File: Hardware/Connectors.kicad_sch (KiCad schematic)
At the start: 22 parts, among them J1 Conn_01x07, J2 Conn_01x03, SW6 SW_Push, SW7 SW_Push

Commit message: Replaced the ISOW1044 CAN Transceiver with the ISO1042 + isolated DC-DC and LDO
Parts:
- renumbered C28 to C22, C29 to C23, FILTER2 to FILTER1, J2 to J1, J1 to J2, R16 to R14, R17 to R15, R13 to R16, R15 to R17, R14 to R18, R18 to R19, TVS5 to TVS3, TVS3 to TVS4, TVS4 to TVS5
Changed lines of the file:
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@@
 		(dnp no)
 		(fields_autoplaced yes)
-		(property "Reference" "#PWR022"
+		(property "Reference" "#PWR024"
 			(at 73.66 198.12 0)
 			(effects
@@
 			(project "CANIO-Board"
 				(path "/a11f98b2-3b09-4cf9-8535-19e509fe91b9/e5b74127-3612-4017-b1e2-26fb10a2adfa"
-					(reference "#PWR022")
+					(reference "#PWR024")
 					(unit 1)
 				)
@@
 		(on_board yes)
 		(dnp no)
-		(property "Reference" "R13"
+		(property "Reference" "R16"
 			(at 40.64 181.61 90)
 			(effects
@@
 			(project "CANIO-Board"
 				(path "/a11f98b2-3b09-4cf9-8535-19e509fe91b9/e5b74127-3612-4017-b1e2-26fb10a2adfa"
-					(reference "R13")
+					(reference "R16")
 					(unit 1)
 				)
@@
 		(dnp no)
 		(fields_autoplaced yes)
-		(property "Reference" "#PWR023"
+		(property "Reference" "#PWR019"
 			(at 118.11 105.41 0)
 			(effects
@@
 			(project "CANIO-Board"
 				(path "/a11f98b2-3b09-4cf9-8535-19e509fe91b9/e5b74127-3612-4017-b1e2-26fb10a2adfa"
-					(reference "#PWR023")
+					(reference "#PWR019")
 					(unit 1)
 				)
@@
 		(dnp no)
 		(fields_autoplaced yes)
-		(property "Reference" "#PWR021"
+		(property "Reference" "#PWR022"
 			(at 59.69 148.59 0)
 			(effects
@@
 			(project "CANIO-Board"
 				(path "/a11f98b2-3b09-4cf9-8535-19e509fe91b9/e5b74127-3612-4017-b1e2-26fb10a2adfa"
-					(reference "#PWR021")
+					(reference "#PWR022")
 					(unit 1)
 				)
@@
 		(on_board yes)
 		(dnp no)
-		(property "Reference" "R16"
+		(property "Reference" "R14"
 			(at 219.456 66.294 90)
 			(effects
@@
 			(project ""
 				(path "/a11f98b2-3b09-4cf9-8535-19e509fe91b9/e5b74127-3612-4017-b1e2-26fb10a2adfa"
-					(reference "R16")
+					(reference "R14")
 					(unit 1)
 				)
@@
 		(dnp no)
 		(fields_autoplaced yes)
-		(property "Reference" "#PWR024"
+		(property "Reference" "#PWR023"
 			(at 132.08 165.1 0)
 			(effects
@@
 			(project "CANIO-Board"
 				(path "/a11f98b2-3b09-4cf9-8535-19e509fe91b9/e5b74127-3612-4017-b1e2-26fb10a2adfa"
-					(reference "#PWR024")
+					(reference "#PWR023")
 					(unit 1)
 				)
@@
 		(on_board yes)
 		(dnp no)
-		(property "Reference" "#PWR025"
+		(property "Reference" "#PWR021"
 			(at 232.41 111.76 0)
 			(effects
@@
 			(project "CANIO-Board"
 				(path "/a11f98b2-3b09-4cf9-8535-19e509fe91b9/e5b74127-3612-4017-b1e2-26fb10a2adfa"
-					(reference "#PWR025")
+					(reference "#PWR021")
 					(unit 1)
 				)
@@
 		(dnp no)
 		(fields_autoplaced yes)
-		(property "Reference" "C28"
+		(property "Reference" "C22"
 			(at 50.8 172.8469 0)
 			(effects
@@
 			(project "CANIO-Board"
 				(path "/a11f98b2-3b09-4cf9-8535-19e509fe91b9/e5b74127-3612-4017-b1e2-26fb10a2adfa"
-					(reference "C28")
+					(reference "C22")
 					(unit 1)
 				)
@@
 		(dnp no)
 		(fields_autoplaced yes)
-		(property "Reference" "J1"
+		(property "Reference" "J2"
 			(at 74.93 71.1199 0)
 			(effects
@@
 			(project ""
 				(path "/a11f98b2-3b09-4cf9-8535-19e509fe91b9/e5b74127-3612-4017-b1e2-26fb10a2adfa"
-					(reference "J1")
+					(reference "J2")
 					(unit 1)
 				)
@@
 		(on_board yes)
 		(dnp no)
-		(property "Reference" "J2"
+		(property "Reference" "J1"
 			(at 129.794 60.452 0)
 			(effects
@@
 			(project ""
 				(path "/a11f98b2-3b09-4cf9-8535-19e509fe91b9/e5b74127-3612-4017-b1e2-26fb10a2adfa"
-					(reference "J2")
+					(reference "J1")
 					(unit 1)
 				)
@@
 		(on_board yes)
 		(dnp no)
-		(property "Reference" "R14"
+		(property "Reference" "R18"
 			(at 52.07 181.61 0)
 			(effects
@@
 			(project "CANIO-Board"
 				(path "/a11f98b2-3b09-4cf9-8535-19e509fe91b9/e5b74127-3612-4017-b1e2-26fb10a2adfa"
-					(reference "R14")
+					(reference "R18")
 					(unit 1)
 				)
@@
 		(on_board yes)
 		(dnp no)
-		(property "Reference" "TVS4"
+		(property "Reference" "TVS5"
 			(at 68.326 91.44 0)
 			(effects
@@
 			(project ""
 				(path "/a11f98b2-3b09-4cf9-8535-19e509fe91b9/e5b74127-3612-4017-b1e2-26fb10a2adfa"
-					(reference "TVS4")
+					(reference "TVS5")
 					(unit 1)
 				)
@@
 		(on_board yes)
 		(dnp no)
-		(property "Reference" "TVS3"
+		(property "Reference" "TVS4"
 			(at 39.878 91.186 0)
 			(effects
@@
 			(project "CANIO-Board"
 				(path "/a11f98b2-3b09-4cf9-8535-19e509fe91b9/e5b74127-3612-4017-b1e2-26fb10a2adfa"
-					(reference "TVS3")
+					(reference "TVS4")
 					(unit 1)
 				)
@@
 		(on_board yes)
 		(dnp no)
-		(property "Reference" "R18"
+		(property "Reference" "R19"
 			(at 52.07 186.69 0)
 			(effects
@@
 			(project "CANIO-Board"
 				(path "/a11f98b2-3b09-4cf9-8535-19e509fe91b9/e5b74127-3612-4017-b1e2-26fb10a2adfa"
-					(reference "R18")
+					(reference "R19")
 					(unit 1)
 				)
@@
 		(on_board yes)
 		(dnp no)
-		(property "Reference" "TVS5"
+		(property "Reference" "TVS3"
 			(at 134.366 90.17 0)
 			(effects
@@
 			(project "CANIO-Board"
 				(path "/a11f98b2-3b09-4cf9-8535-19e509fe91b9/e5b74127-3612-4017-b1e2-26fb10a2adfa"
-					(reference "TVS5")
+					(reference "TVS3")
 					(unit 1)
 				)
@@
 		(on_board yes)
 		(dnp no)
-		(property "Reference" "R15"
+		(property "Reference" "R17"
 			(at 73.66 176.53 90)
 			(effects
@@
 			(project "CANIO-Board"
 				(path "/a11f98b2-3b09-4cf9-8535-19e509fe91b9/e5b74127-3612-4017-b1e2-26fb10a2adfa"
-					(reference "R15")
+					(reference "R17")
 					(unit 1)
 				)
@@
 		(dnp no)
 		(fields_autoplaced yes)
-		(property "Reference" "C29"
+		(property "Reference" "C23"
 			(at 82.55 184.2769 0)
 			(effects
@@
 			(project "CANIO-Board"
 				(path "/a11f98b2-3b09-4cf9-8535-19e509fe91b9/e5b74127-3612-4017-b1e2-26fb10a2adfa"
-					(reference "C29")
+					(reference "C23")
 					(unit 1)
 				)
@@
 		(dnp no)
 		(fields_autoplaced yes)
-		(property "Reference" "FILTER2"
+		(property "Reference" "FILTER1"
 			(at 196.85 74.93 0)
 			(effects
@@
 			(project ""
 				(path "/a11f98b2-3b09-4cf9-8535-19e509fe91b9/e5b74127-3612-4017-b1e2-26fb10a2adfa"
-					(reference "FILTER2")
+					(reference "FILTER1")
 					(unit 1)
 				)
@@
 		(on_board yes)
 		(dnp no)
-		(property "Reference" "R17"
+		(property "Reference" "R15"
 			(at 219.456 68.834 90)
 			(effects
@@
 			(project "CANIO-Board"
 				(path "/a11f98b2-3b09-4cf9-8535-19e509fe91b9/e5b74127-3612-4017-b1e2-26fb10a2adfa"
-					(reference "R17")
-					(unit 1)
-				)
+					(reference "R15")
+					(unit 1)
+				)

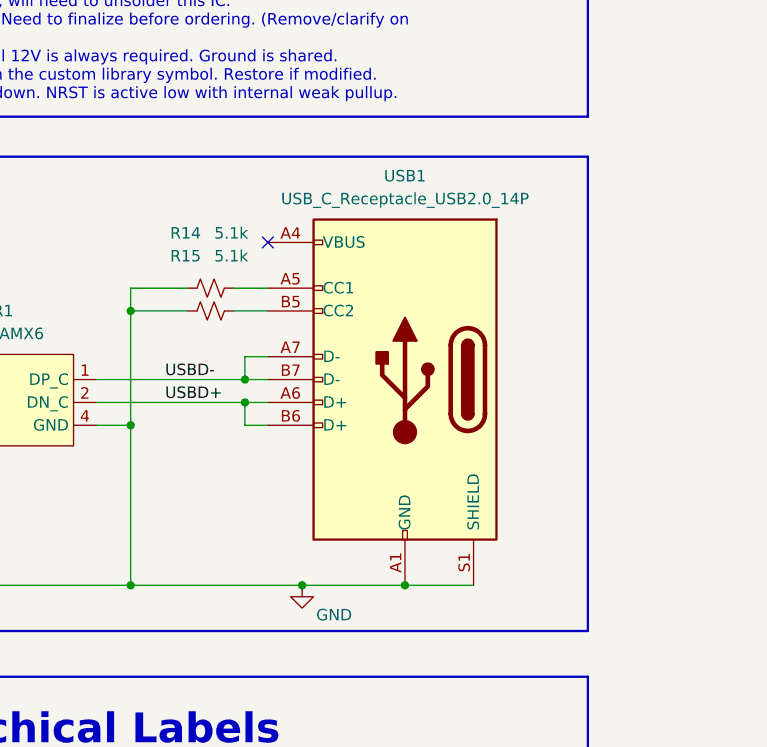
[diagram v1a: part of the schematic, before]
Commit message: Updated the USB-C connector from 14 pin to 16 pin
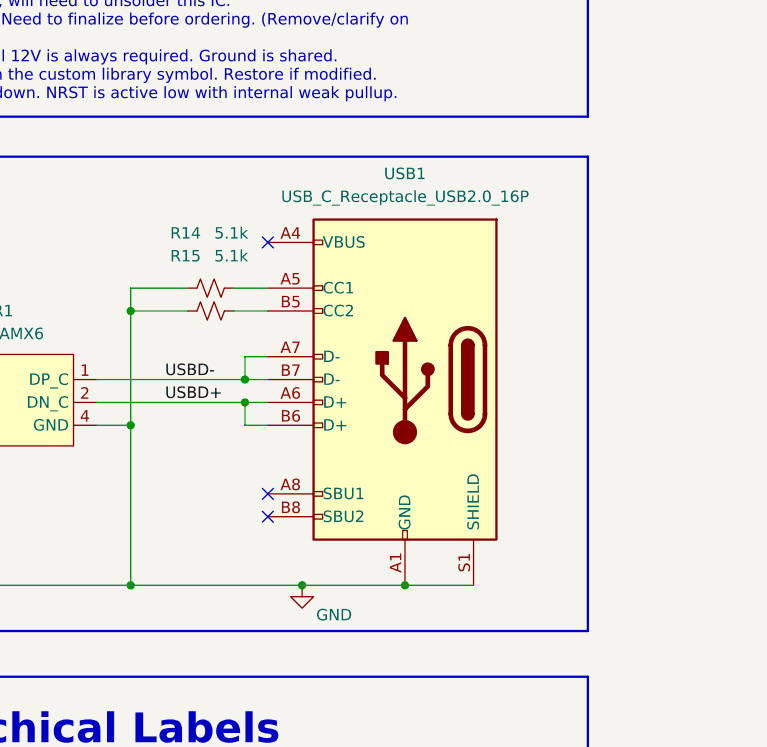
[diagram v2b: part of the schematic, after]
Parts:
- removed USB1: USB_C_Receptacle_USB2.0_14P, symbol Connector:USB_C_Receptacle_USB2.0_14P
- added USB1: USB_C_Receptacle_USB2.0_16P, symbol Connector:USB_C_Receptacle_USB2.0_16P
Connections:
- net GND: now also USB1.A1 (GND), USB1.A12 (GND), USB1.B1 (GND), USB1.B12 (GND), USB1.S1 (SHIELD)
- net USBD+: now also USB1.A6 (D+), USB1.B6 (D+)
- net USBD-: now also USB1.A7 (D-), USB1.B7 (D-)
- net at R14.2: now also USB1.A5 (CC1)
- net at R15.2: now also USB1.B5 (CC2)
- new net: USB1.A4 (VBUS), USB1.A9 (VBUS), USB1.B4 (VBUS), USB1.B9 (VBUS)
- no-connect marks 3 -> 5
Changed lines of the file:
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@@
 	)
 	(junction
+		(at 243.84 105.41)
+		(diameter 0)
+		(color 0 0 0 0)
+	)
+	(junction
 		(at 130.81 73.66)
 		(diameter 0)
@@
 	)
 	(junction
-		(at 243.84 105.41)
-		(diameter 0)
-		(color 0 0 0 0)
-	)
-	(junction
 		(at 133.35 36.83)
 		(diameter 0)
@@
 	)
 	(no_connect
+		(at 228.6 97.79)
+	)
+	(no_connect
+		(at 228.6 95.25)
+	)
+	(no_connect
 		(at 43.18 82.55)
 	)
@@
 	(wire
 		(pts
-			(xy 251.46 105.41) (xy 243.84 105.41)
+			(xy 232.41 105.41) (xy 243.84 105.41)
 		)
 		(stroke
@@
 	(wire
 		(pts
+			(xy 243.84 105.41) (xy 251.46 105.41)
+		)
+		(stroke
+			(width 0)
+			(type default)
+		)
+	)
+	(wire
+		(pts
 			(xy 120.65 148.59) (xy 134.62 148.59)
 		)
@@
 	(wire
 		(pts
-			(xy 232.41 105.41) (xy 243.84 105.41)
-		)
-		(stroke
-			(width 0)
-			(type default)
-		)
-	)
-	(wire
-		(pts
 			(xy 106.68 76.2) (xy 106.68 78.74)
 		)
@@
 	)
 	(symbol
-		(lib_id "Connector_Generic:Conn_01x04")
-		(at 66.04 133.35 0)
+		(lib_id "Connector:USB_C_Receptacle_USB2.0_16P")
+		(at 243.84 82.55 0)
+		(mirror y)
 		(unit 1)
 		(exclude_from_sim no)
@@
 		(on_board yes)
 		(dnp no)
-		(fields_autoplaced yes)
-		(property "Reference" "WAGO1"
-			(at 68.58 133.3499 0)
+		(property "Reference" "USB1"
+			(at 243.84 59.69 0)
 			(effects
 				(font
 					(size 1.27 1.27)
 				)
-				(justify left)
 			)
 		)
-		(property "Value" "2606"
-			(at 68.58 135.8899 0)
+		(property "Value" "USB_C_Receptacle_USB2.0_16P"
+			(at 243.84 62.23 0)
 			(effects
 				(font
 					(size 1.27 1.27)
 				)
-				(justify left)
 			)
 		)
 		(property "Footprint" ""
-			(at 66.04 133.35 0)
+			(at 240.03 82.55 0)
 			(effects
 				(font
@@
 			)
 		)
-		(property "Datasheet" "~"
-			(at 66.04 133.35 0)
+		(property "Datasheet" "https://www.usb.org/sites/default/files/documents/usb_type-c.zip"
+			(at 240.03 82.55 0)
 			(effects
 				(font
@@
 			)
 		)
-		(property "Description" "Generic connector, single row, 01x04, script generated (kicad-library-utils/schlib/autogen/connector/)"
-			(at 66.04 133.35 0)
+		(property "Description" "USB 2.0-only 16P Type-C Receptacle connector"
+			(at 243.84 82.55 0)
 			(effects
 				(font
@@
 			)
 		)
-		(pin "2"
+		(pin "A5"
 		)
-		(pin "1"
+		(pin "S1"
 		)
-		(pin "3"
+		(pin "B12"
 		)
-		(pin "4"
+		(pin "B9"
+		)
+		(pin "A7"
+		)
+		(pin "A9"
+		)
+		(pin "A6"
+		)
+		(pin "A12"
+		)
+		(pin "A4"
+		)
+		(pin "A1"
+		)
+		(pin "B1"
+		)
+		(pin "B7"
+		)
+		(pin "B6"
+		)
+		(pin "A8"
+		)
+		(pin "B8"
+		)
+		(pin "B5"
+		)
+		(pin "B4"
 		)
 		(instances
 			(project ""
 				(path "/a11f98b2-3b09-4cf9-8535-19e509fe91b9/e5b74127-3612-4017-b1e2-26fb10a2adfa"
-					(reference "WAGO1")
+					(reference "USB1")
 					(unit 1)
 				)
@@
 	)
 	(symbol
-		(lib_id "power:GND")
-		(at 132.08 158.75 0)
+		(lib_id "Connector_Generic:Conn_01x04")
+		(at 66.04 133.35 0)
 		(unit 1)
 		(exclude_from_sim no)
@@
 		(dnp no)
 		(fields_autoplaced yes)
-		(property "Reference" "#PWR023"
-			(at 132.08 165.1 0)
+		(property "Reference" "WAGO1"
+			(at 68.58 133.3499 0)
 			(effects
 				(font
 					(size 1.27 1.27)
 				)
-				(hide yes)
+				(justify left)
 			)
 		)
-		(property "Value" "GND"
-			(at 132.08 163.83 0)
+		(property "Value" "2606"
+			(at 68.58 135.8899 0)
 			(effects
 				(font
 					(size 1.27 1.27)
 				)
+				(justify left)
 			)
 		)
 		(property "Footprint" ""
-			(at 132.08 158.75 0)
+			(at 66.04 133.35 0)
 			(effects
 				(font
@@
 			)
 		)
-		(property "Datasheet" ""
-			(at 132.08 158.75 0)
+		(property "Datasheet" "~"
+			(at 66.04 133.35 0)
 			(effects
 				(font
@@
 			)
 		)
-		(property "Description" "Power symbol creates a global label with name \"GND\" , ground"
-			(at 132.08 158.75 0)
+		(property "Description" "Generic connector, single row, 01x04, script generated (kicad-library-utils/schlib/autogen/connector/)"
+			(at 66.04 133.35 0)
 			(effects
 				(font
@@
 			)
 		)
+		(pin "2"
+		)
 		(pin "1"
 		)
+		(pin "3"
+		)
+		(pin "4"
+		)
 		(instances
-			(project "CANIO-Board"
+			(project ""
 				(path "/a11f98b2-3b09-4cf9-8535-19e509fe91b9/e5b74127-3612-4017-b1e2-26fb10a2adfa"
-					(reference "#PWR023")
+					(reference "WAGO1")
 					(unit 1)
 				)
@@
 	)
 	(symbol
-		(lib_id "Connector:USB_C_Receptacle_USB2.0_14P")
-		(at 243.84 82.55 0)
-		(mirror y)
+		(lib_id "power:GND")
+		(at 132.08 158.75 0)
 		(unit 1)
 		(exclude_from_sim no)
@@
 		(on_board yes)
 		(dnp no)
-		(property "Reference" "USB1"
-			(at 243.84 59.944 0)
+		(fields_autoplaced yes)
+		(property "Reference" "#PWR023"
+			(at 132.08 165.1 0)
 			(effects
 				(font
 					(size 1.27 1.27)
 				)
+				(hide yes)
 			)
 		)
-		(property "Value" "USB_C_Receptacle_USB2.0_14P"
-			(at 243.84 62.484 0)
+		(property "Value" "GND"
+			(at 132.08 163.83 0)
 			(effects
 				(font
@@
 		)
 		(property "Footprint" ""
-			(at 240.03 82.55 0)
+			(at 132.08 158.75 0)
 			(effects
 				(font
@@
 			)
 		)
-		(property "Datasheet" "https://www.usb.org/sites/default/files/documents/usb_type-c.zip"
-			(at 240.03 82.55 0)
+		(property "Datasheet" ""
+			(at 132.08 158.75 0)
 			(effects
 				(font
@@
 			)
 		)
-		(property "Description" "USB 2.0-only 14P Type-C Receptacle connector"
-			(at 243.84 82.55 0)
+		(property "Description" "Power symbol creates a global label with name \"GND\" , ground"
+			(at 132.08 158.75 0)
 			(effects
 				(font
@@
 			)
 		)
-		(pin "B6"
-		)
-		(pin "A12"
-		)
-		(pin "B12"
-		)
-		(pin "A7"
-		)
-		(pin "B4"
-		)
-		(pin "A4"
-		)
-		(pin "A9"
-		)
-		(pin "A6"
-		)
-		(pin "A1"
-		)
-		(pin "B1"
-		)
-		(pin "B5"
-		)
-		(pin "B7"
-		)
-		(pin "S1"
-		)
-		(pin "A5"
-		)
-		(pin "B9"
+		(pin "1"
 		)
 		(instances
-			(project ""
+			(project "CANIO-Board"
 				(path "/a11f98b2-3b09-4cf9-8535-19e509fe91b9/e5b74127-3612-4017-b1e2-26fb10a2adfa"
-					(reference "USB1")
+					(reference "#PWR023")
 					(unit 1)
 				)
